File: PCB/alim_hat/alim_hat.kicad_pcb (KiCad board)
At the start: 2 copper layers, 85 x 56 mm, 42 parts, among them J1 Screw_Terminal_01x04, J10 Conn_01x02, J11 Conn_01x02, J12 Conn_01x02, J2 Barrel_Jack_MountingPin, J3 Conn_02x04_Odd_Even, J4 Jack-DC, J5 Jack-DC, J6 Jack-DC, J7 Jack-DC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

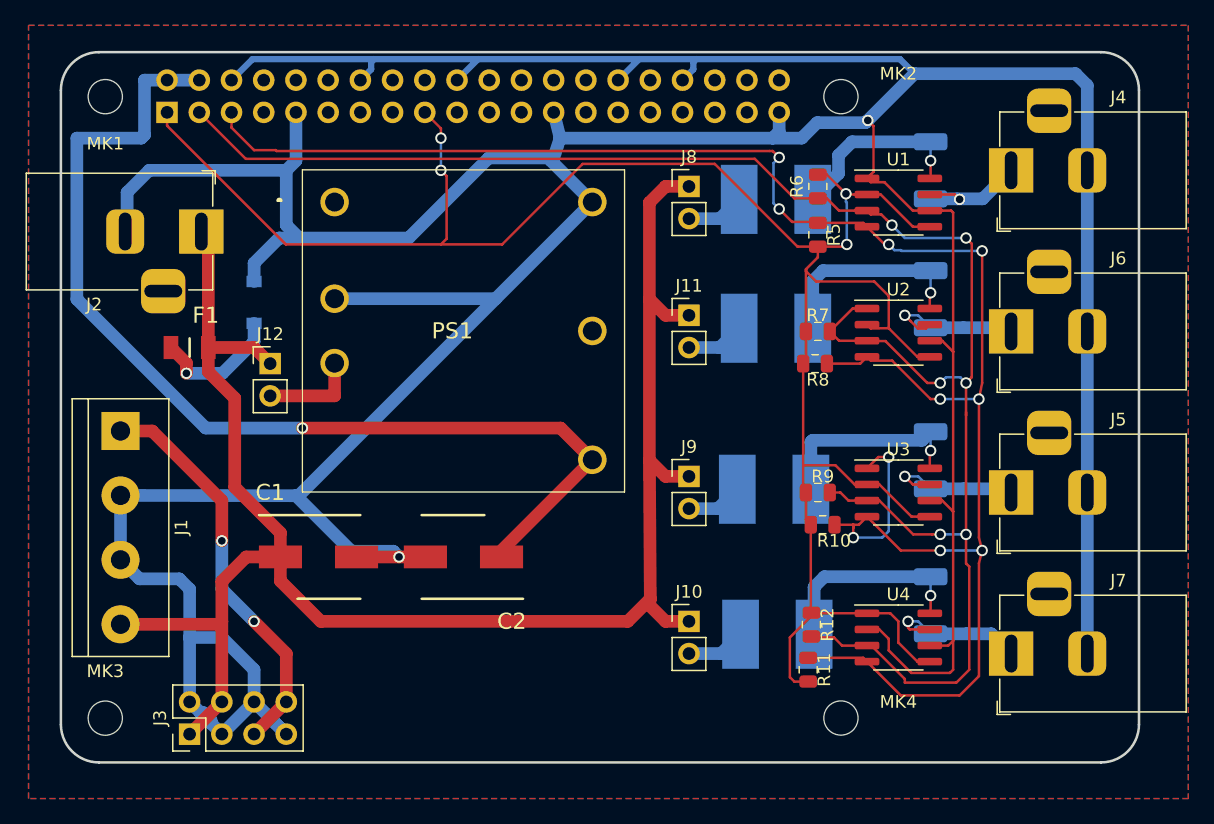
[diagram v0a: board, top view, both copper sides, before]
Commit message: upgrade alim piste size on alim board
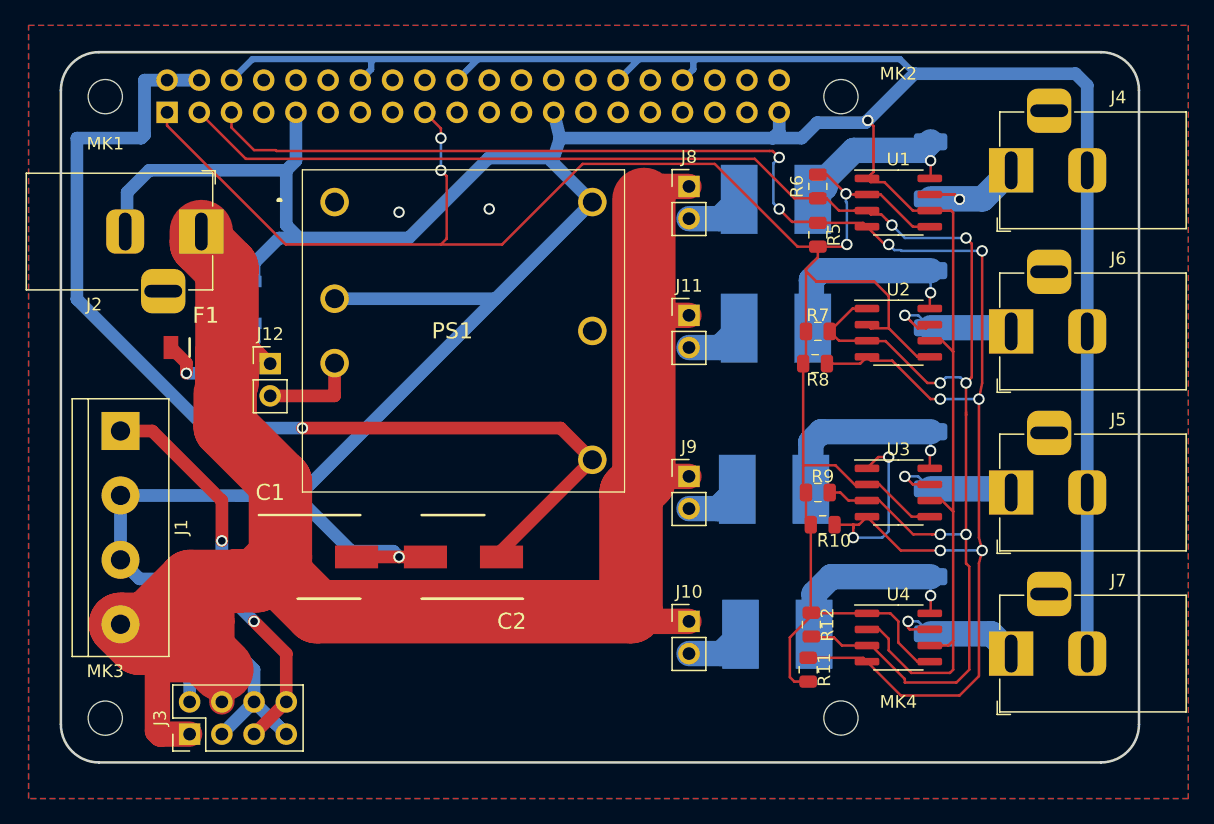
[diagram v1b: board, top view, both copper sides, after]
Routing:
- net +12V: track 139.8 -> 280.6 mm
- net GND: track 400.7 -> 396.9 mm, vias 2 -> 4
- added copper zone on B.Cu, net GND
- added copper zone on F.Cu, net GND
- removed copper zone on B.Cu, net (none)
- removed copper zone on F.Cu, net (none)

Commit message: add  lcls part number and add Fab file
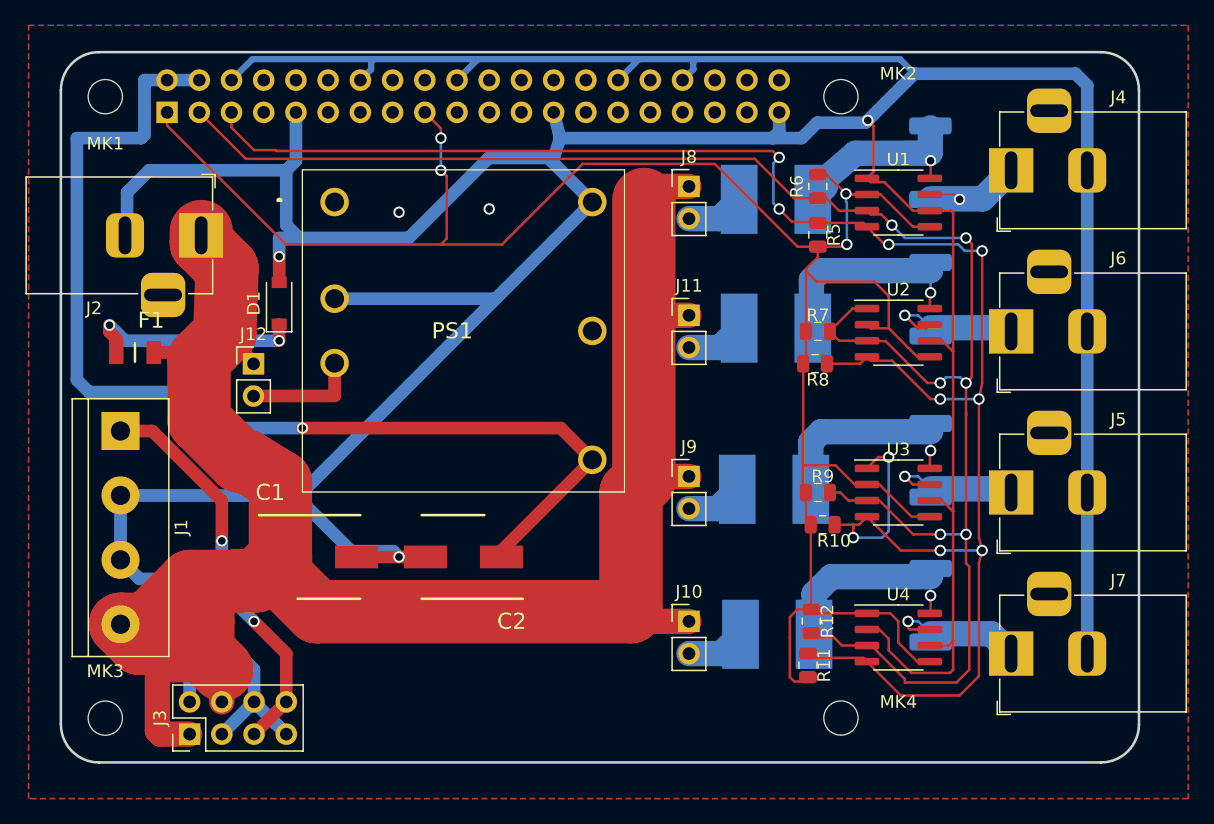
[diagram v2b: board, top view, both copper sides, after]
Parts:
- D1: moved to F.Cu
- J2: value Barrel_Jack_MountingPin -> Jack-DC
- R1, R2, R3, R4: value 0.02 -> 0.02 1W; footprint Resistor_SMD:R_2010_5025Metric -> Resistor_SMD:R_2512_6332Metric
- moved F1 4.33 mm to (205.9, 117.4)
- moved D1 1.98 mm to (217.2, 113.5)
- moved J12 1.31 mm to (215.2, 118.3)
- moved R1 0.61 mm to (268.6, 102.4)
- moved R11 0.35 mm to (258.9, 142.0)
- moved J2 0.30 mm to (211.1, 108.1)
- moved R12 0.26 mm to (259.2, 138.6)
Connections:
- P1 pad 10: (no net) -> /UART_RX
- P1 pad 11: (no net) -> /GPIO17
- P1 pad 12: (no net) -> /GPIO18
- P1 pad 13: (no net) -> /GPIO27
- P1 pad 15: (no net) -> /GPIO22
- P1 pad 16: (no net) -> /GPIO23
- P1 pad 18: (no net) -> /GPIO24
- P1 pad 19: (no net) -> Net-(P1-Pad19)
- P1 pad 21: (no net) -> Net-(P1-Pad21)
- P1 pad 22: (no net) -> /GPIO25
- P1 pad 23: (no net) -> Net-(P1-Pad23)
- P1 pad 24: (no net) -> Net-(P1-Pad24)
- P1 pad 26: (no net) -> Net-(P1-Pad26)
- P1 pad 27: (no net) -> Net-(P1-Pad27)
- P1 pad 28: (no net) -> Net-(P1-Pad28)
- P1 pad 29: (no net) -> /GPIO5
- P1 pad 31: (no net) -> /GPIO6
- P1 pad 32: (no net) -> /GPIO12(PWM0)
- P1 pad 33: (no net) -> /GPIO13(PWM1)
- P1 pad 35: (no net) -> Net-(P1-Pad35)
- P1 pad 36: (no net) -> /GPIO16
- P1 pad 37: (no net) -> /GPIO26
- P1 pad 38: (no net) -> Net-(P1-Pad38)
- P1 pad 40: (no net) -> Net-(P1-Pad40)
- P1 pad 7: (no net) -> /1-wire
- P1 pad 8: (no net) -> /UART_TX
- PS1 pad 1: (no net) -> Net-(PS1-Pad1)
- PS1 pad 5: (no net) -> Net-(PS1-Pad5)
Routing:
- net Net-(D1-Pad1): track 10.4 -> 17.6 mm, vias 1 -> 2
- net +5V: track 83.3 -> 87.1 mm
- net Net-(J12-Pad2): track 7.66 -> 8.97 mm
- net GND: track 396.9 -> 396.1 mm, vias 4 -> 5
- net +3V3: track 166.4 -> 167.2 mm
- net +12V: track 280.6 -> 281.3 mm

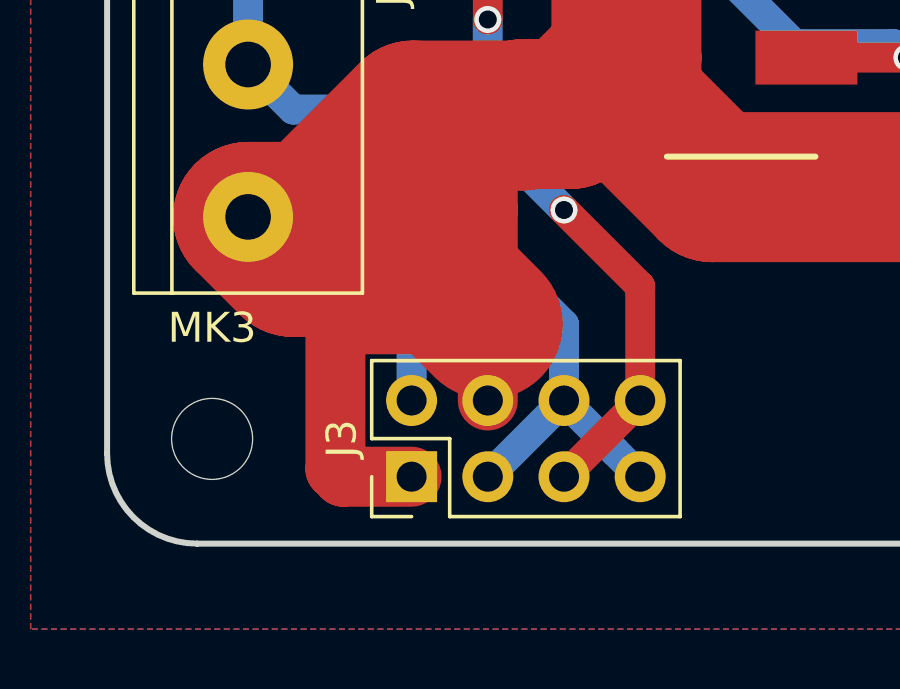
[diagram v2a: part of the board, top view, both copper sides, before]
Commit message: warning : correct big error on alim hat
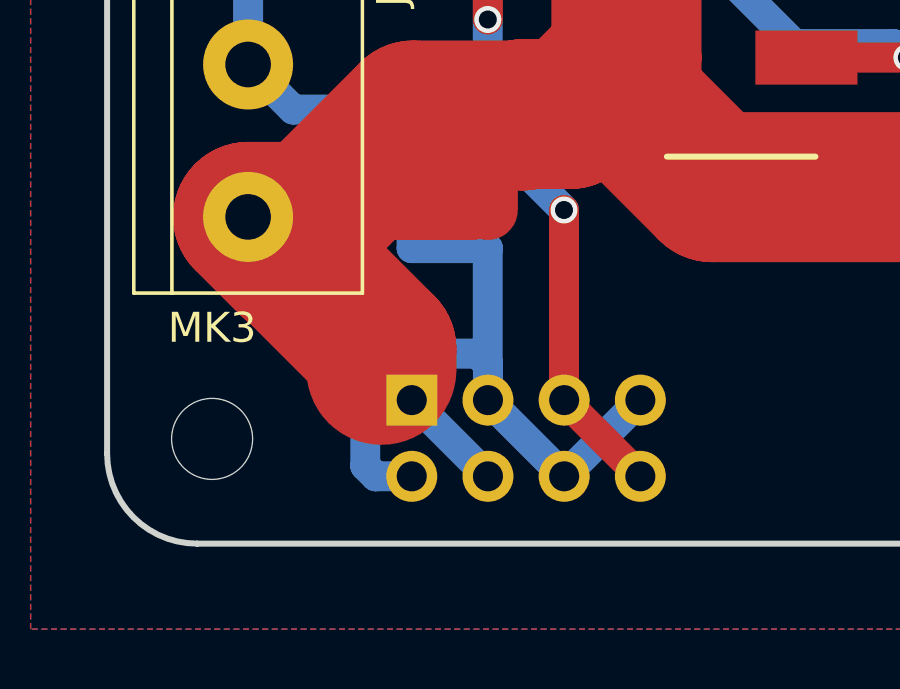
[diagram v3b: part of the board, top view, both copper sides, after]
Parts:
- J3: moved to B.Cu
- moved J3 2.55 mm to (210.2, 144.9), turned to 270 degrees
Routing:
- net +12V: track 281.3 -> 263.9 mm
- net VCC: track 31.8 -> 30.8 mm
- net GND: track 396.1 -> 397.1 mm

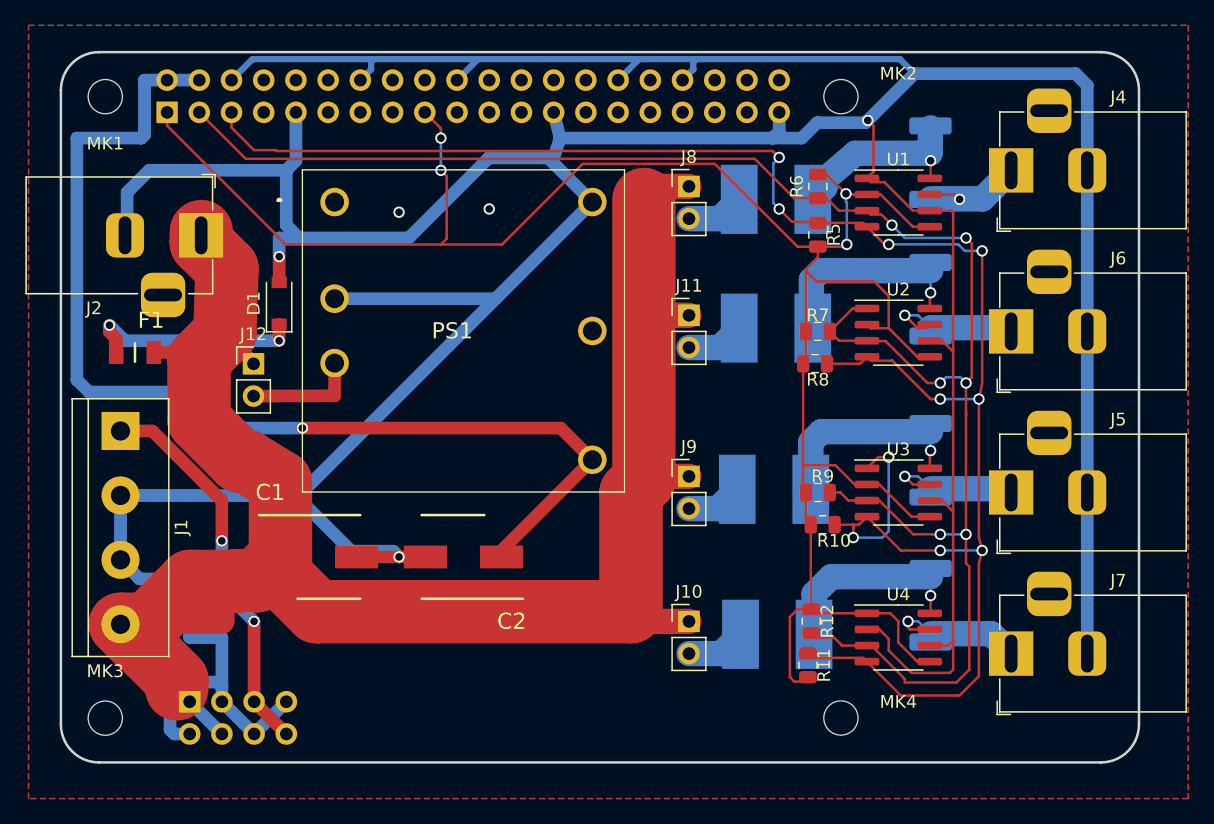
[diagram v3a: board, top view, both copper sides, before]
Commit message: change DC for XT30, change controle res for pwm
add ds1050Z-025+ change for xt30 connector for in alim
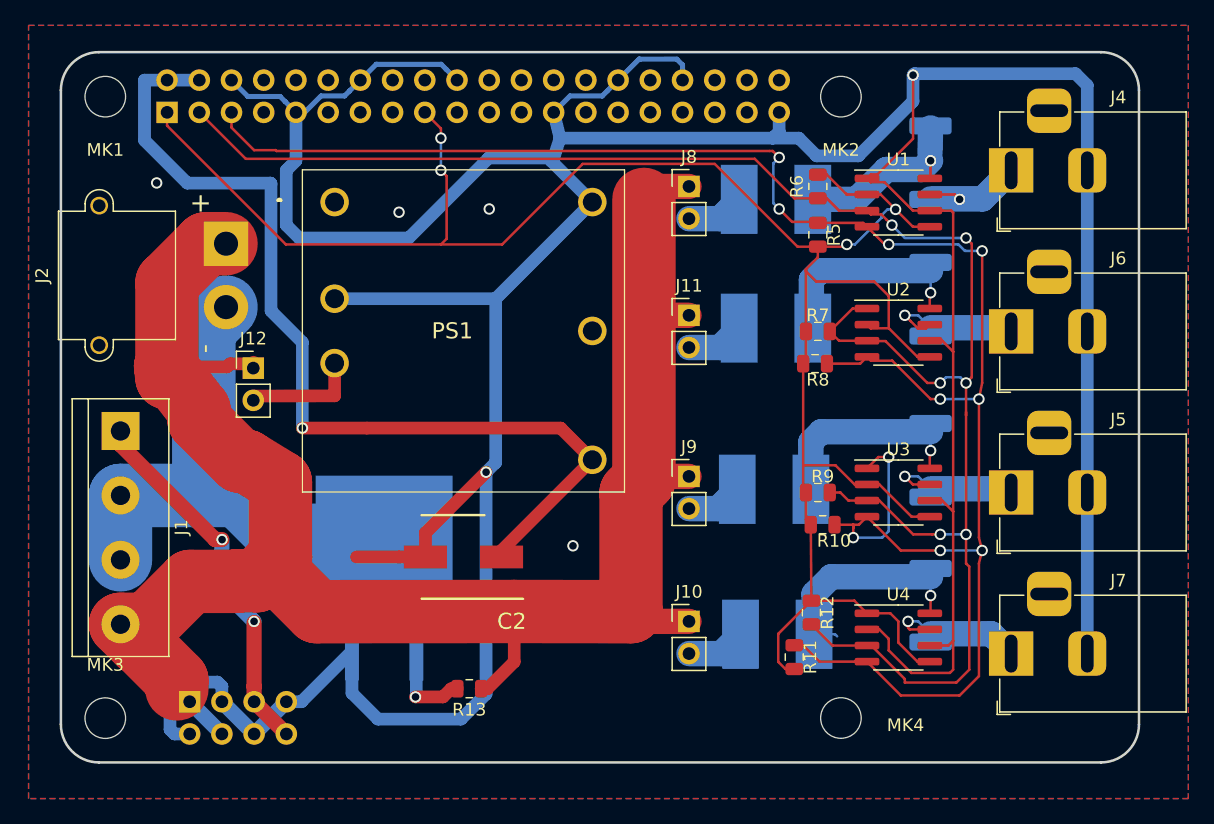
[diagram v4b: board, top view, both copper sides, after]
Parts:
- removed C1: 100uF, capa:CAPAE660X800N
- removed D1: B140HW-7, Diode_SMD:D_SOD-123
- removed F1: Polyfuse_Small, fuse:FUSC3216X100N
- added Q1: IRFS7530TRLPBF, Package_TO_SOT_SMD:TO-263-2, B.Cu at (225.5, 135.2)
- added R13: 1k, Resistor_SMD:R_0805_2012Metric, F.Cu at (232.2, 143.9)
- J2: footprint Connector_BarrelJack:BarrelJack_Horizontal -> Connector_AMASS:AMASS_XT30PW-M_1x02_P2.50mm_Horizontal
- MK1, MK2, MK3, MK4: footprint MountingHole:MountingHole_2.7mm_M2.5 -> MountingHole:MountingHole_3.2mm_M3
- moved J2 2.07 mm to (213.0, 108.8), turned to 90 degrees
- moved R11 1.26 mm to (257.8, 141.4)
- moved R12 0.69 mm to (259.2, 137.9)
- moved J12 0.34 mm to (215.2, 118.6)
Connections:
- J1 pad 2: GND -> /gnd_no
- J1 pad 3: GND -> /gnd_no
- J2 pad 2: GND -> /gnd_no
- P1 pad 10: /UART_RX -> (no net)
- P1 pad 11: /GPIO17 -> (no net)
- P1 pad 12: /GPIO18 -> (no net)
- P1 pad 13: /GPIO27 -> (no net)
- P1 pad 15: /GPIO22 -> (no net)
- P1 pad 16: /GPIO23 -> (no net)
- P1 pad 18: /GPIO24 -> (no net)
- P1 pad 19: Net-(P1-Pad19) -> (no net)
- P1 pad 21: Net-(P1-Pad21) -> (no net)
- P1 pad 22: /GPIO25 -> (no net)
- P1 pad 23: Net-(P1-Pad23) -> (no net)
- P1 pad 24: Net-(P1-Pad24) -> (no net)
- P1 pad 26: Net-(P1-Pad26) -> (no net)
- P1 pad 27: Net-(P1-Pad27) -> (no net)
- P1 pad 28: Net-(P1-Pad28) -> (no net)
- P1 pad 29: /GPIO5 -> (no net)
- P1 pad 31: /GPIO6 -> (no net)
- P1 pad 32: /GPIO12(PWM0) -> (no net)
- P1 pad 33: /GPIO13(PWM1) -> (no net)
- P1 pad 35: Net-(P1-Pad35) -> (no net)
- P1 pad 36: /GPIO16 -> (no net)
- P1 pad 37: /GPIO26 -> (no net)
- P1 pad 38: Net-(P1-Pad38) -> (no net)
- P1 pad 40: Net-(P1-Pad40) -> (no net)
- P1 pad 7: /1-wire -> (no net)
- P1 pad 8: /UART_TX -> (no net)
- PS1 pad 1: Net-(PS1-Pad1) -> (no net)
- PS1 pad 5: Net-(PS1-Pad5) -> (no net)
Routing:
- net GND: track 397.1 -> 348.5 mm, vias 5 -> 6
- net /gnd_no: track 0.00 -> 47.0 mm
- net +12V: track 263.9 -> 244.7 mm
- net Net-(D1-Pad1): track 17.6 -> 0.00 mm, vias 2 -> 0
- net +5V: track 87.1 -> 75.3 mm
- net Net-(Q1-Pad1): track 0.00 -> 7.20 mm, vias 0 -> 1
- net VCC: track 30.8 -> 35.7 mm
- net Net-(F5-Pad2): track 15.8 -> 17.7 mm
- net /SCL: track 154.9 -> 156.4 mm
- net /SDA: track 142.0 -> 142.6 mm

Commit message: add serigraph and update name for componant
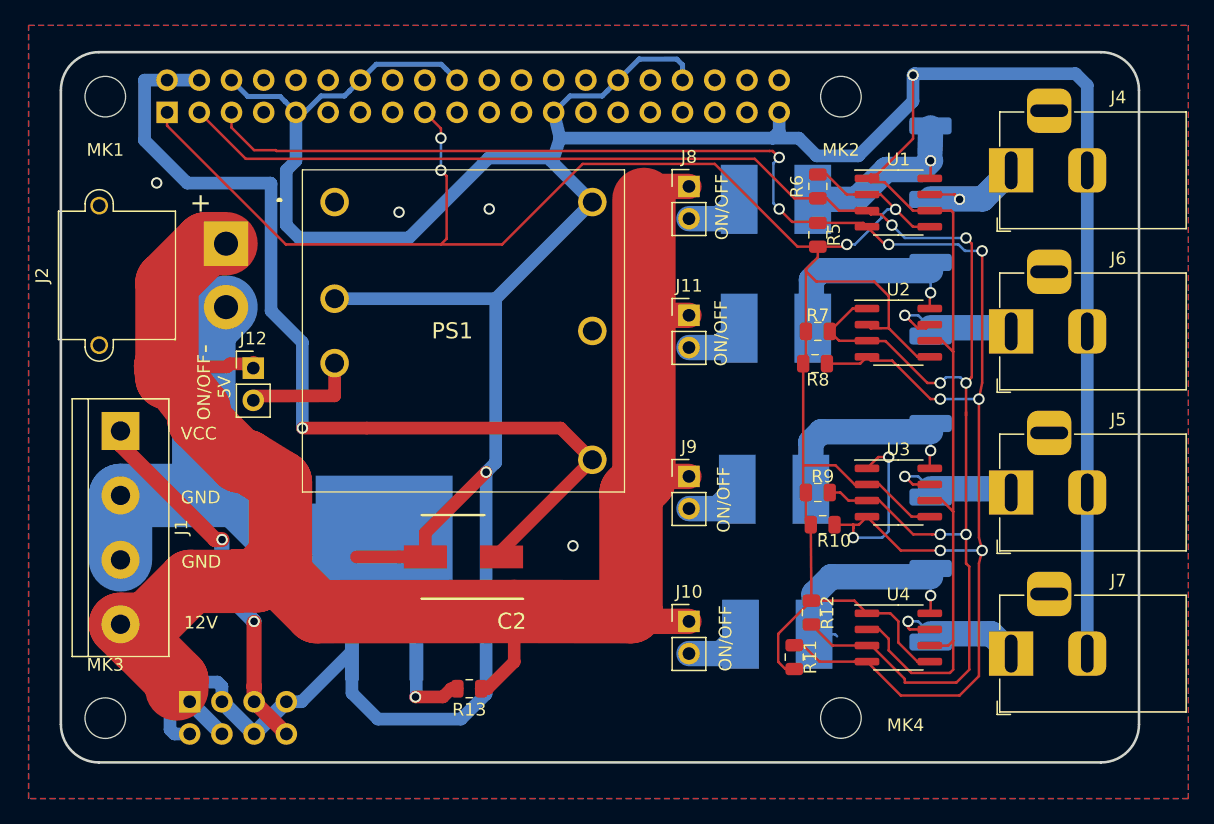
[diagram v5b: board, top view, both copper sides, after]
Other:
- board text added: "12V"
- board text added: "GND"
- board text added: "ON/OFF"
- board text added: "ON/OFF 5V"
- board text added: "VCC"
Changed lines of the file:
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@@
   (general
     (thickness 1.6)
-    (drawings 8)
+    (drawings 17)
     (tracks 505)
     (zones 0)
@@
       (rotate (xyz 90 0 90))
     )
+  )
+  (gr_text "ON/OFF\n5V" (at 212.10056 120.10166 90) (layer F.SilkS)
+    (effects (font (size 1 1) (thickness 0.15)))
+  )
+  (gr_text 12V (at 211.05408 138.66906) (layer F.SilkS)
+    (effects (font (size 1 1) (thickness 0.15)))
+  )
+  (gr_text GND (at 211.08202 133.87862) (layer F.SilkS)
+    (effects (font (size 1 1) (thickness 0.15)))
+  )
+  (gr_text GND (at 211.02614 128.79862) (layer F.SilkS)
+    (effects (font (size 1 1) (thickness 0.15)))
+  )
+  (gr_text VCC (at 210.87628 123.76688) (layer F.SilkS)
+    (effects (font (size 1 1) (thickness 0.15)))
+  )
+  (gr_text ON/OFF (at 252.12588 105.90306 90) (layer F.SilkS)
+    (effects (font (size 1 1) (thickness 0.15)))
+  )
+  (gr_text ON/OFF (at 252.05476 115.85224 90) (layer F.SilkS)
+    (effects (font (size 1 1) (thickness 0.15)))
+  )
+  (gr_text ON/OFF (at 252.26558 128.97388 90) (layer F.SilkS)
+    (effects (font (size 1 1) (thickness 0.15)))
+  )
+  (gr_text ON/OFF (at 252.40782 139.91112 90) (layer F.SilkS)
+    (effects (font (size 1 1) (thickness 0.15)))
   )
   (gr_line (start 200.0101 96.6915) (end 200.0101 146.6915) (layer Edge.Cuts) (width 0.2))
@@
   (segment (start 270.104 142.634) (end 270.358 142.38) (width 0.2) (layer F.Cu) (net 3))
   (segment (start 263.865 103.345) (end 263.565 103.645) (width 0.2) (layer F.Cu) (net 3))
-  (segment (start 226.220001 133.040001) (end 222.918001 133.040001) (width 1) (layer B.Cu) (net 21))
-  (segment (start 226.67 133.49) (end 226.220001 133.040001) (width 1) (layer B.Cu) (net 21))
   (segment (start 217.78 103.01) (end 217.78 107.328) (width 1) (layer B.Cu) (net 3))
   (segment (start 217.78 107.328) (end 218.796 108.344) (width 1) (layer B.Cu) (net 3))
@@
   (segment (start 221.59 120.79) (end 215.19682 120.80524) (width 1) (layer F.Cu) (net 20))
   (segment (start 221.59 118.21) (end 221.59 120.79) (width 1) (layer F.Cu) (net 20))
+  (segment (start 226.220001 133.040001) (end 222.918001 133.040001) (width 1) (layer B.Cu) (net 21))
+  (segment (start 226.67 133.49) (end 226.220001 133.040001) (width 1) (layer B.Cu) (net 21))
   (segment (start 204.71 133.72) (end 204.71 128.64) (width 5) (layer B.Cu) (net 21))
   (segment (start 217.131204 131.7787) (end 213.992504 128.64) (width 5) (layer B.Cu) (net 21))
